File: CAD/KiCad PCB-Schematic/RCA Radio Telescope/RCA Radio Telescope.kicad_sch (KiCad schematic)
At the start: 11 parts, among them J1 USB_A, J2 USB_B_Micro, U1 ZX60-P33ULN+, U2 ADALM Pluto SDR

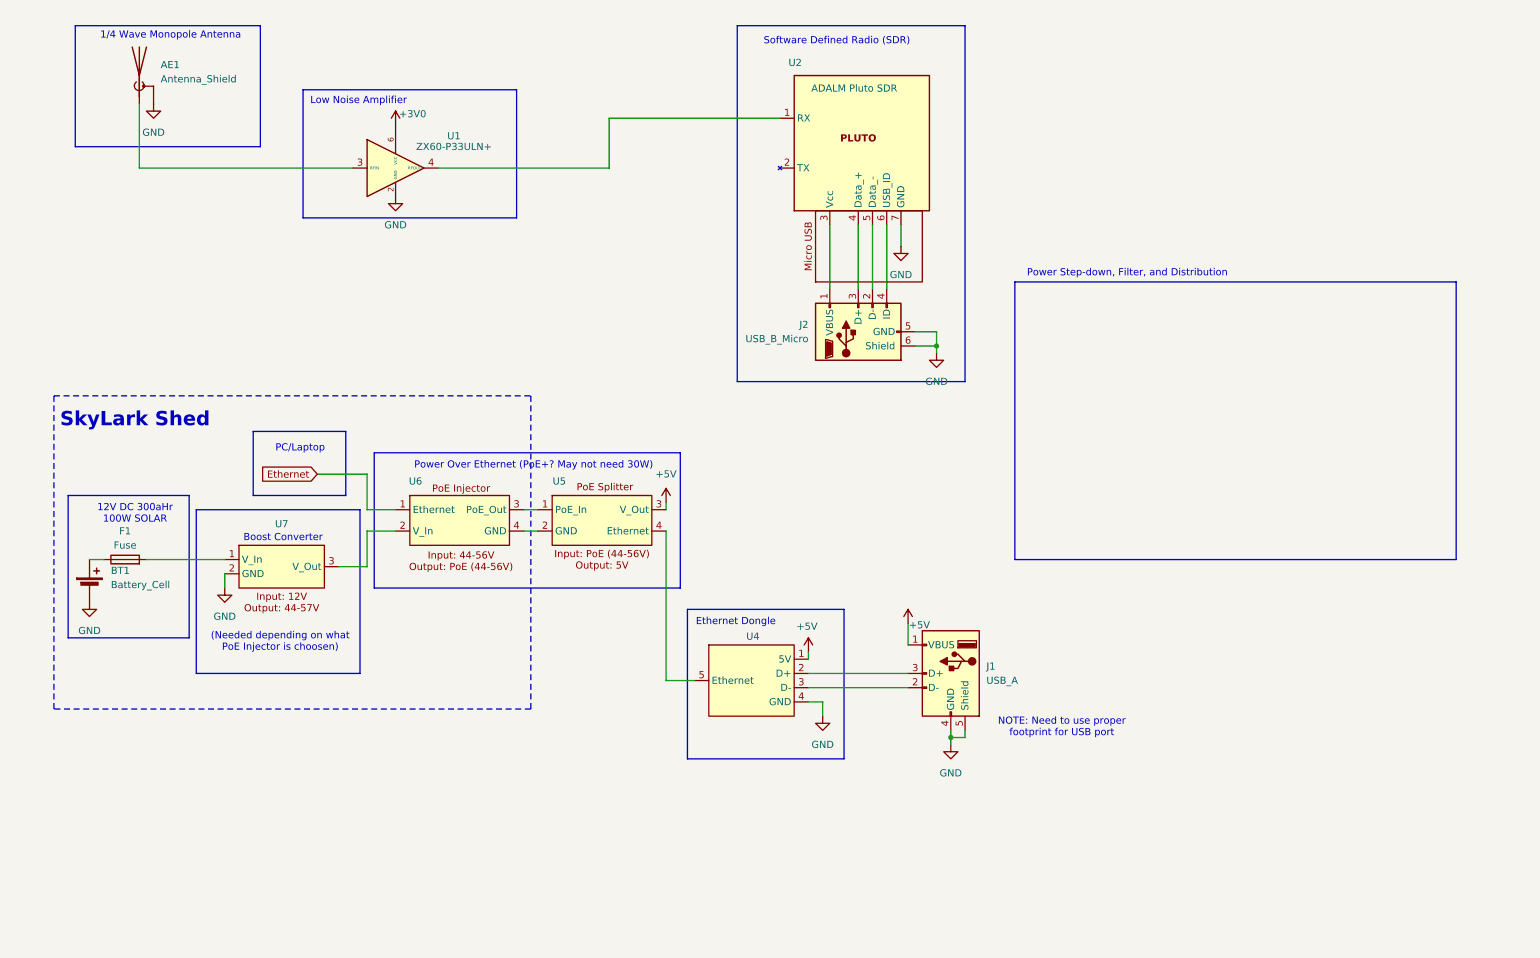
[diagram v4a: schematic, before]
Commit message: Updated Schematic
Updated System Schematic to v1.3
-Add Hierarchal Schematics for Filters and Power/Data Distribution

Updated Filters Schematic to v1.0
- Added circuitry for RF switching, level shifting, and power supply.
- Added placeholders for filters

Updated Power/Data Distribution Schematic to v1.0
- Added placeholders for input and output voltage
- Added placeholders for stepdown and power filters
- Added USBA connectors for Ethernet and SDR connectivity
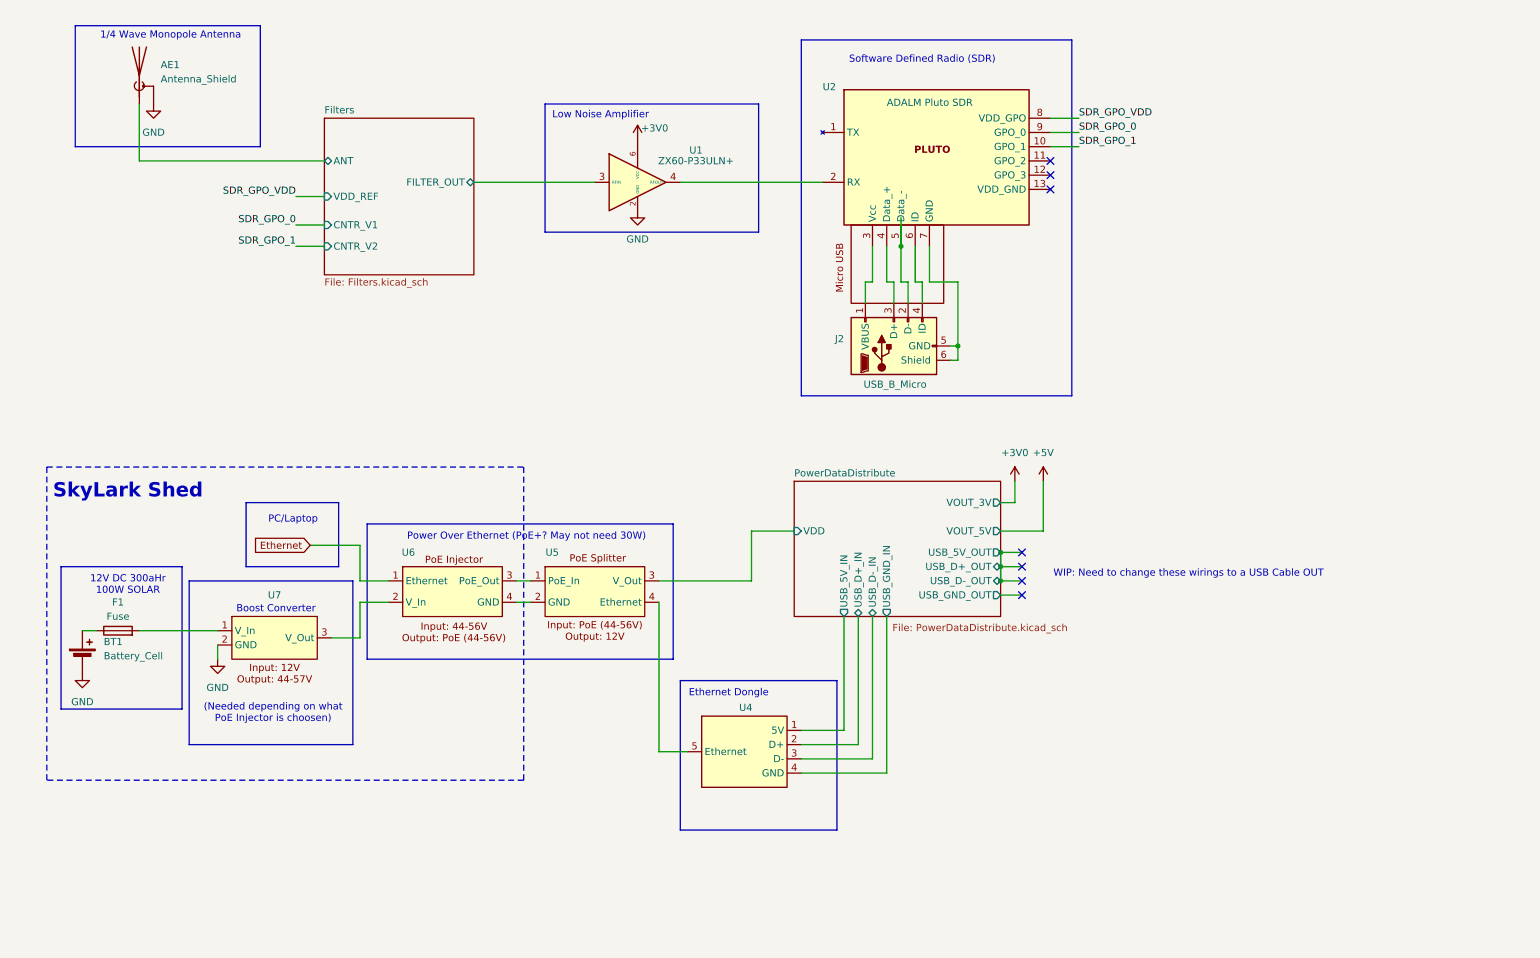
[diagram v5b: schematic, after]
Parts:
- removed J1: USB_A, symbol Connector:USB_A
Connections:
- net +5V: no longer U4.1 (5V), U5.3 (V_Out)
- net GND: no longer J2.5 (GND), J2.6 (Shield), U2.7 (GND), U4.4 (GND)
- net at U2.1 (TX): no longer U1.4 (RFOUT)
- net at U2.2 (RX): now also U1.4 (RFOUT)
- net Filters/ANT: now reaches AE1.1 (A)
- net Filters/ANT: no longer U1.3 (RFIN)
- net PowerDataDistribute/USB_D-_IN: now reaches U4.3 (D-)
- net PowerDataDistribute/USB_D+_IN: now reaches U4.2 (D+)
- new net: J2.5 (GND), J2.6 (Shield), U2.7 (GND)
- new net Filters/FILTER_OUT: U1.3 (RFIN)
- new net PowerDataDistribute/USB_5V_IN: U4.1 (5V)
- new net PowerDataDistribute/USB_GND_IN: U4.4 (GND)
- new net PowerDataDistribute/VDD: U5.3 (V_Out)
- new net SDR_GPO_0: U2.9 (GPO_0)
- new net SDR_GPO_1: U2.10 (GPO_1)
- new net SDR_GPO_VDD: U2.8 (VDD_GPO)
- no-connect marks 0 -> 7
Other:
- added sheet Filters (Filters.kicad_sch)
- added sheet PowerDataDistribute (PowerDataDistribute.kicad_sch)
- note added: "WIP: Need to change these wirings to a USB Cable OUT"
- note removed: "NOTE: Need to use proper footprint for USB port"
- note removed: "Power Step-down, Filter, and Distribution"
- title: (none) -> RCA Radio Telescope System
- moved on the sheet: BT1, F1, J2, U1, U4, U5, U6, U7

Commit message: Updated Schematic
Updated Root Schematic to v1.4
- Added Screw Terminals for 5V In/Out, 3V Out for LNA
- Reorganized Skylark Shed Power to include Battery, Inverter, and AC-DC Adapter
- Added TODO list

Updated PowerDataDistribute Schematic to v1.1
- Removed labels for USB signals and replaced it with single USB_OUT signal
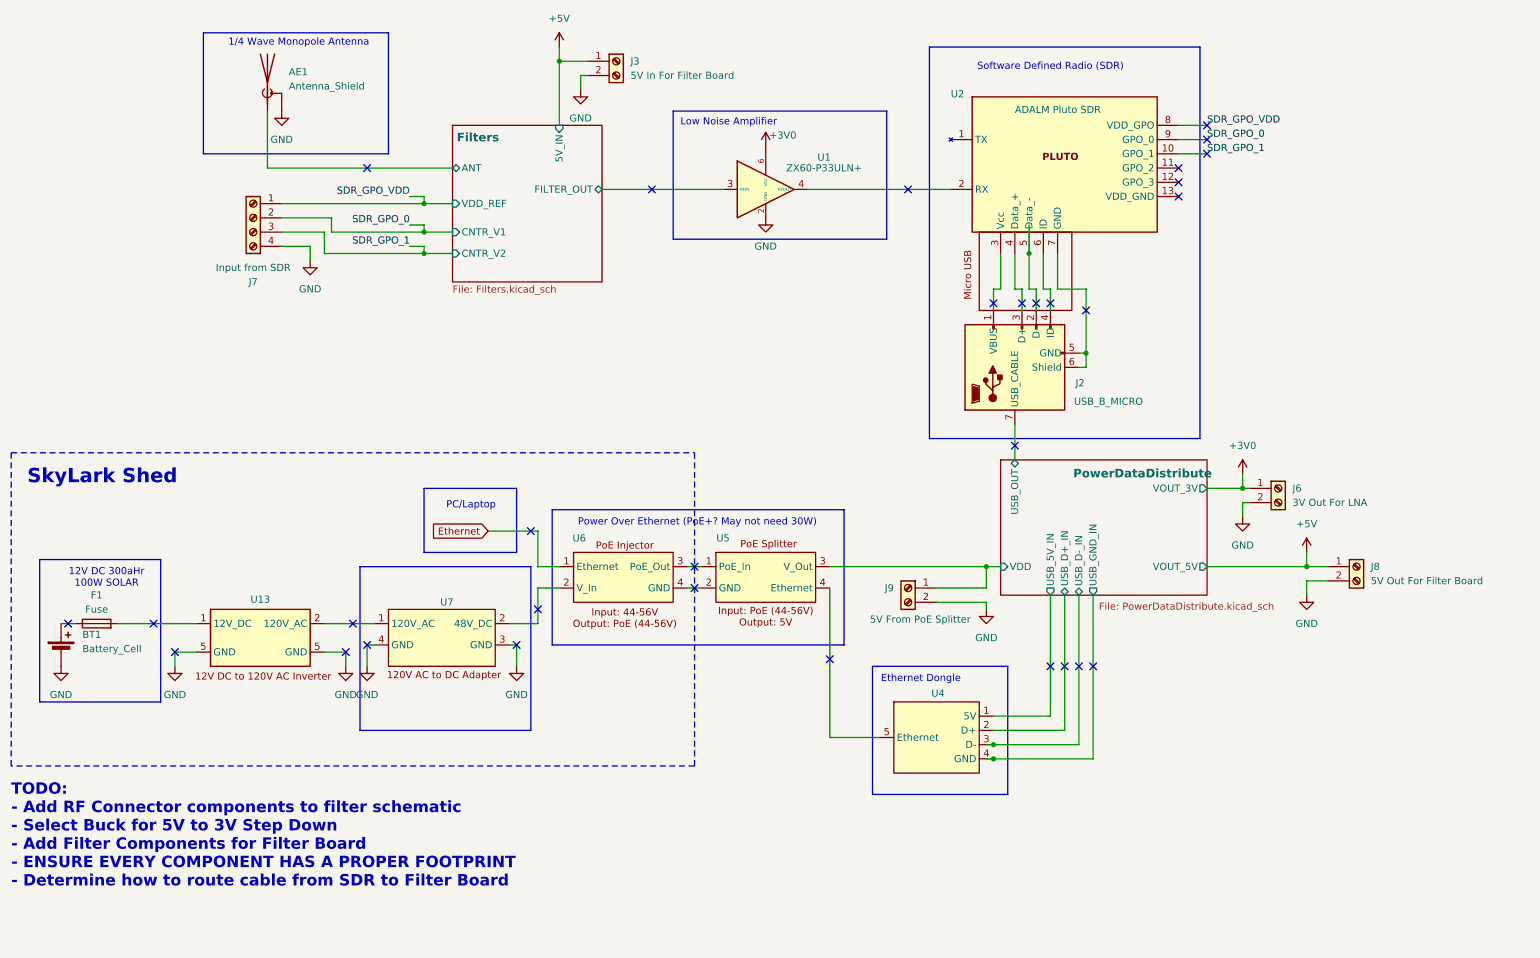
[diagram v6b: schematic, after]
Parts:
- removed J2: USB_B_Micro, symbol Connector:USB_B_Micro
- removed U7: ~, symbol Radio Telescope:Boost_Converter
- added J2: USB_B_MICRO, symbol Radio Telescope:USB_A_wCable
- added J3: 5V In For Filter Board, symbol Connector:Screw_Terminal_01x02
- added J6: 3V Out For LNA, symbol Connector:Screw_Terminal_01x02
- added J7: Input from SDR, symbol Connector:Screw_Terminal_01x04
- added J8: 5V Out For Filter Board, symbol Connector:Screw_Terminal_01x02
- added J9: 5V From PoE Splitter, symbol Connector:Screw_Terminal_01x02
- added U13: ~, symbol Radio Telescope:12DCto120AC-Inverter
- added U7: ~, symbol Radio Telescope:48v-wall-outlet
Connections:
- net +3V0: now also J6.1 (Pin_1)
- net +5V: now also J3.1 (Pin_1), J8.1 (Pin_1)
- net GND: now also J3.2 (Pin_2), J6.2 (Pin_2), J7.4 (Pin_4), J8.2 (Pin_2), J9.2 (Pin_2), U13.5 (GND), U7.3 (GND), U7.4 (GND)
- net PowerDataDistribute/VDD: now also J9.1 (Pin_1)
- net SDR_GPO_0: now also J7.2 (Pin_2)
- net SDR_GPO_1: now also J7.3 (Pin_3)
- net SDR_GPO_VDD: now also J7.1 (Pin_1)
- net at U2.3 (Vcc): now also J2.1 (VBUS)
- net at U2.4 (Data_+): now also J2.3 (D+)
- net at U2.5 (Data_-): now also J2.2 (D-)
- net at U2.6 (ID): now also J2.4 (ID)
- net at U2.7 (GND): now also J2.5 (GND), J2.6 (Shield)
- net at F1.2: now also U13.1 (12V_DC)
- net at U6.2 (V_In): now also U7.2 (48V_DC)
- new net: U13.2 (120V_AC), U7.1 (120V_AC)
- new net PowerDataDistribute/USB_OUT: J2.7 (USB_CABLE)
- no-connect marks 7 -> 31
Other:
- sheet Filters ports: added 5V_IN; removed none
- sheet PowerDataDistribute ports: added USB_OUT; removed USB_5V_OUT, USB_D+_OUT, USB_D-_OUT, USB_GND_OUT
- note added: "TODO: - Add RF Connector components to filter schematic - Select Buck for 5V to 3V Step Down - Add Filter Components for Filter Board - ENSURE EVERY COMPONENT HAS A PROPER FOOTPRINT - Determine how to route cable from SDR to Filter Board"
- note removed: "(Needed depending on what PoE Injector is choosen)"
- note removed: "Boost Converter"
- note removed: "WIP: Need to change these wirings to a USB Cable OUT"
- moved on the sheet: AE1, BT1, F1, U1, U2, U4, U5, U6
